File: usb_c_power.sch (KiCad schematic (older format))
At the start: 27 parts, among them J1 USB4085-GF-A, J2 ‎282837-2‎, Q1 IRF9358TRPBF, U1 CYPD3177

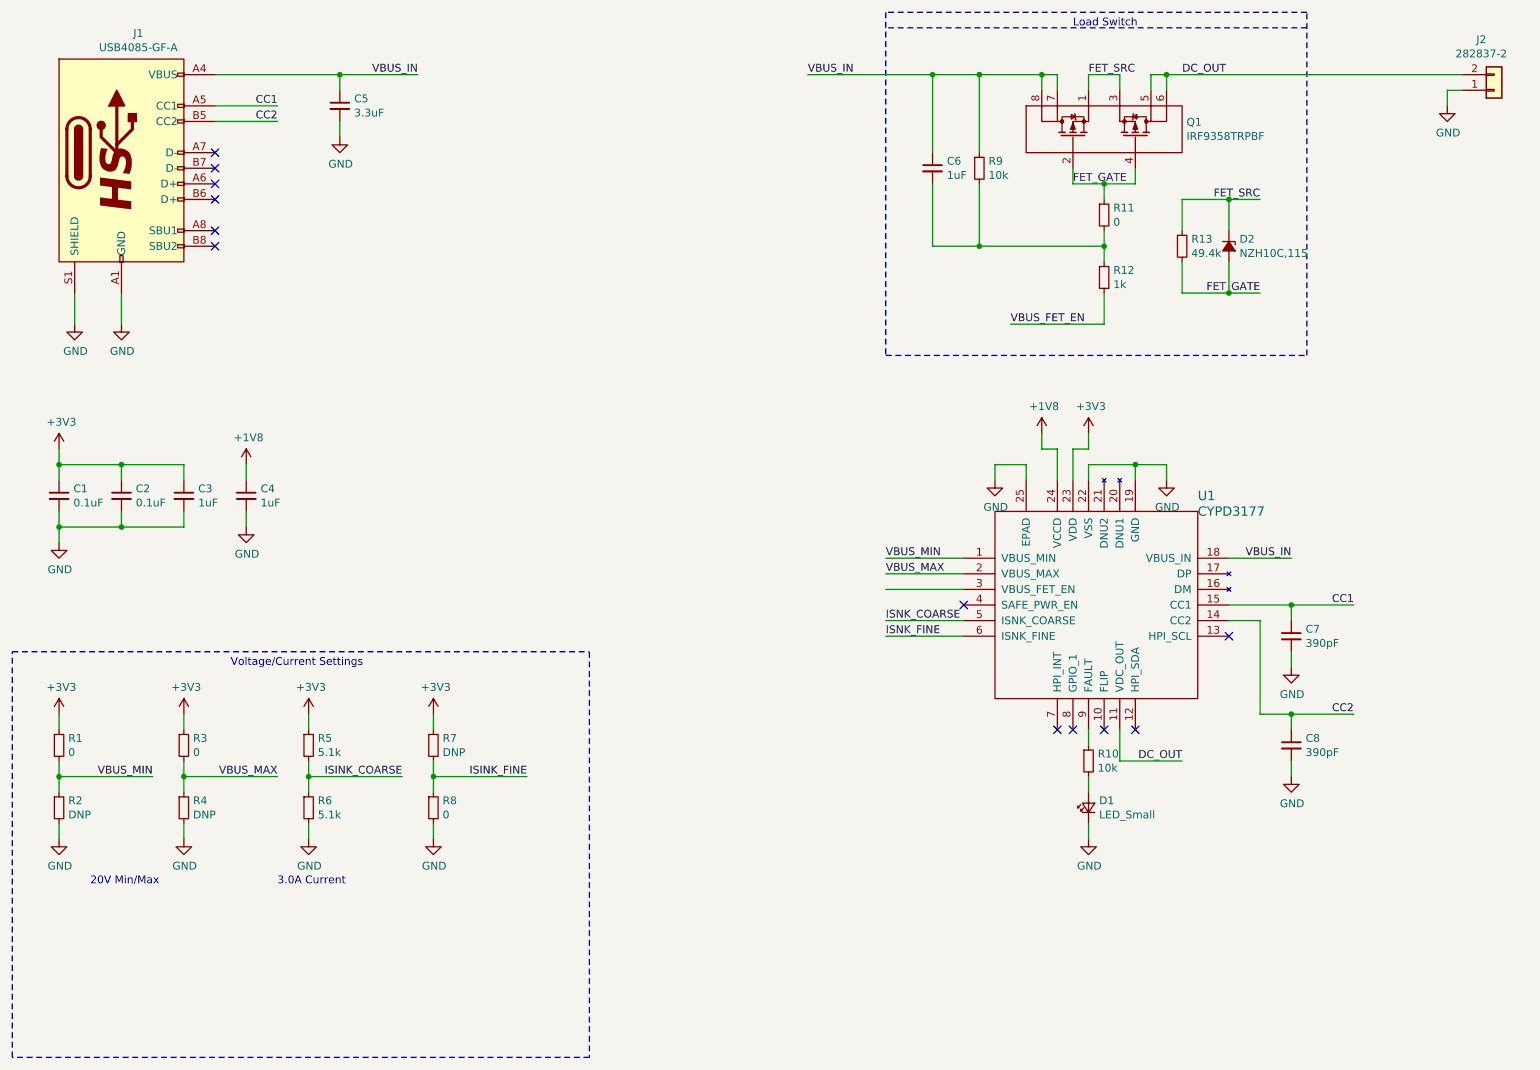
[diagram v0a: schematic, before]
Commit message: Schematic tentatively finished.
Footprints assigned and component details added
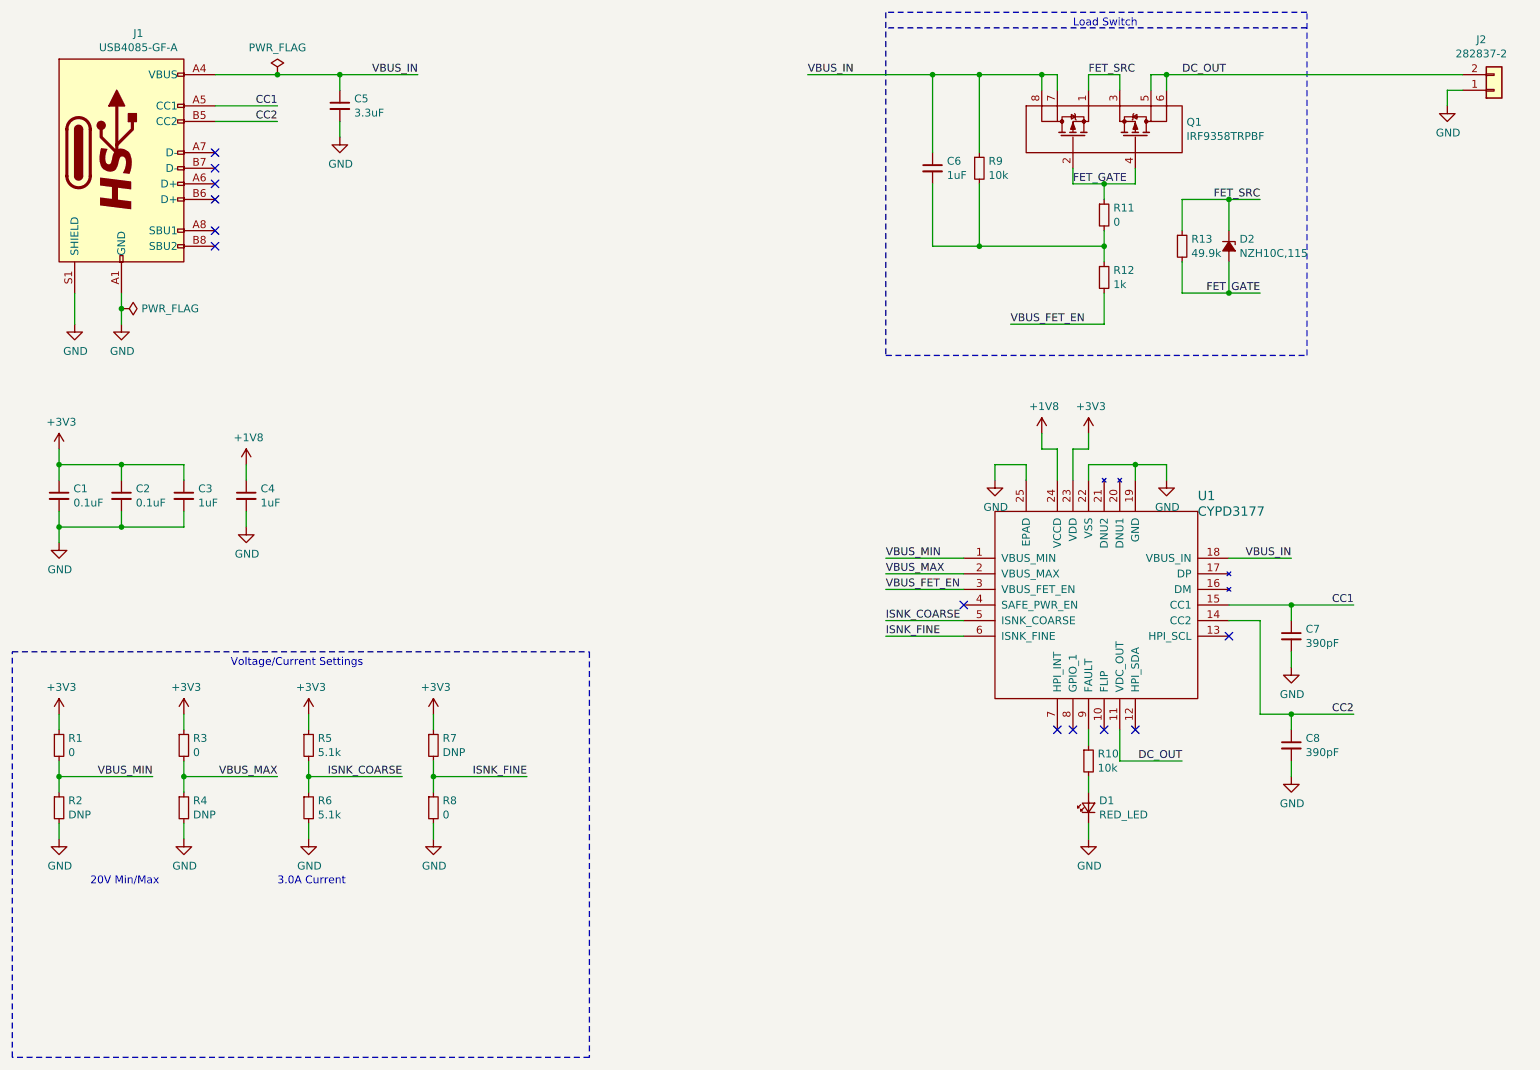
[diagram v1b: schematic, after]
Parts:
- C1, C2: footprint (none) -> Capacitor_SMD:C_0402_1005Metric; DKPN (none) -> 490-1318-1-ND; MPN (none) -> GRM155R61A104KA01D; Voltage - Rated (none) -> 10V
- C3, C4: footprint (none) -> Capacitor_SMD:C_0402_1005Metric; DKPN (none) -> 1276-1067-1-ND; MPN (none) -> CL05A105KO5NNNC; Voltage - Rated (none) -> 16V
- C5: footprint (none) -> Capacitor_SMD:C_1210_3225Metric; DKPN (none) -> 445-5716-1-ND; MPN (none) -> CGA6P3X7R1H335K250AB; Voltage - Rated (none) -> 50V
- C6: footprint (none) -> Capacitor_SMD:C_0402_1005Metric; DKPN (none) -> 445-175218-1-ND; MPN (none) -> C1005X5R1V105K050BE; Voltage - Rated (none) -> 35V
- C7, C8: footprint (none) -> Capacitor_SMD:C_0402_1005Metric; DKPN (none) -> 1276-1560-1-ND; MPN (none) -> CL05B391KB5NNNC
- D1: value LED_Small -> RED_LED; footprint (none) -> LED_SMD:LED_0603_1608Metric; DKPN (none) -> SML-D12U1WT86CT-ND; MPN (none) -> SML-D12U1WT86
- D2: footprint (none) -> Diode_SMD:D_SOD-123F; DKPN (none) -> 1727-5057-1-ND; MPN (none) -> NZH10C,115
- J1: footprint (none) -> alvarop:USB4085-GF-A; DKPN (none) -> 2073-USB4085-GF-ACT-ND; MPN (none) -> USB4085-GF-A
- J2: footprint (none) -> alvarop:‎282837-2‎; DKPN (none) -> A113320-ND; MPN (none) -> 282837-2
- Q1: footprint (none) -> Package_SO:SO-8_3.9x4.9mm_P1.27mm; DKPN (none) -> IRF9358TRPBFCT-ND; MPN (none) -> IRF9358TRPBF
- R1, R11, R3, R8: footprint (none) -> Resistor_SMD:R_0402_1005Metric; DKPN (none) -> 1276-3480-1-ND; MPN (none) -> RC1005J000CS
- R10, R9: footprint (none) -> Resistor_SMD:R_0402_1005Metric; DKPN (none) -> 311-10KJRCT-ND; MPN (none) -> RC0402JR-0710KL
- R12: footprint (none) -> Resistor_SMD:R_0402_1005Metric; DKPN (none) -> A106129CT-ND; MPN (none) -> CRG0402J1K0
- R13: value 49.4k -> 49.9k; footprint (none) -> Resistor_SMD:R_0402_1005Metric; DKPN (none) -> 311-49.9KLRCT-ND; MPN (none) -> RC0402FR-0749K9L
- R2, R4, R7: footprint (none) -> Resistor_SMD:R_0402_1005Metric
- R5, R6: footprint (none) -> Resistor_SMD:R_0402_1005Metric; DKPN (none) -> 311-5.1KJRCT-ND; MPN (none) -> RC0402JR-075K1L
- U1: footprint (none) -> Package_DFN_QFN:QFN-24-1EP_4x4mm_P0.5mm_EP2.8x2.8mm; DKPN (none) -> 428-4652-ND; MPN (none) -> CYPD3177-24LQXQ
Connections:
- net ISINK_COARSE is gone; now on net ISNK_COARSE: R5.2, R6.1
- net ISINK_FINE is gone; now on net ISNK_FINE: R7.2, R8.1
- net VBUS_FET_EN: now also U1.3 (VBUS_FET_EN)

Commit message: Created v1.1 * much larger (0805) setting resistors * 5A rated USB-C connector * Smaller 10V zener * Paste-in-hole for usb-c
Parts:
- removed J1: USB4085-GF-A, alvarop:USB4085-GF-A, symbol alvarop:USB_C_Receptacle_NODIFFPAIRS
- removed R11: 0, Resistor_SMD:R_0402_1005Metric, symbol Device:R_Small
- added J1: USB_C_Receptacle, alvarop:MOLEX-1054500101, symbol Connector:USB_C_Receptacle
- D2: footprint Diode_SMD:D_SOD-123F -> Diode_SMD:D_0402_1005Metric
- R1, R2, R3, R4, R5, R6, R7, R8: footprint Resistor_SMD:R_0402_1005Metric -> Resistor_SMD:R_0805_2012Metric_Pad1.15x1.40mm_HandSolder
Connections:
- net CC1: now also J1.A5 (CC1)
- net CC2: now also J1.B5 (CC2)
- net FET_GATE: now also C6.2, R12.1, R9.2
- net GND: now also J1.A1 (GND), J1.A12 (GND), J1.B1 (GND), J1.B12 (GND), J1.S1 (SHIELD)
- net VBUS_IN: now also J1.A4 (VBUS), J1.A9 (VBUS), J1.B4 (VBUS), J1.B9 (VBUS)
- no-connect marks 12 -> 20
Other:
- moved on the sheet: C1, C2, C3, C4

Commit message: Finished v1.1 and ordered from oshpark
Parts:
- D2: value NZH10C,115 -> BZT52C10LP-7; DKPN 1727-5057-1-ND -> BZT52C10LPDICT-ND; MPN NZH10C,115 -> BZT52C10LP-7
- R1, R3, R8: DKPN 1276-3480-1-ND -> RMCF0805ZT0R00CT-ND; MPN RC1005J000CS -> RMCF0805ZT0R00
- R5, R6: DKPN 311-5.1KJRCT-ND -> RMCF0805JT5K10CT-ND; MPN RC0402JR-075K1L -> RMCF0805JT5K10
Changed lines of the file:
@@
 Sheet 1 1
 Title "USB-C Power"
-Date "2020-03-21"
+Date "2020-03-23"
 Rev "1.1"
 Comp "alvarop.com"
@@
 P 8700 2200
 F 0 "D2" V 8654 2268 50  0000 L CNN
-F 1 "NZH10C,115" V 8745 2268 50  0000 L CNN
+F 1 "BZT52C10LP-7" V 8745 2268 50  0000 L CNN
 F 2 "Diode_SMD:D_0402_1005Metric" V 8700 2200 50  0001 C CNN
 F 3 "~" V 8700 2200 50  0001 C CNN
-F 4 "1727-5057-1-ND" H 8700 2200 50  0001 C CNN "DKPN"
-F 5 "NZH10C,115" H 8700 2200 50  0001 C CNN "MPN"
+F 4 "BZT52C10LPDICT-ND" H 8700 2200 50  0001 C CNN "DKPN"
+F 5 "BZT52C10LP-7" H 8700 2200 50  0001 C CNN "MPN"
 	1    8700 2200
 	0    1    1    0
@@
 F 2 "Resistor_SMD:R_0805_2012Metric_Pad1.15x1.40mm_HandSolder" H 1200 5400 50  0001 C CNN
 F 3 "~" H 1200 5400 50  0001 C CNN
-F 4 "1276-3480-1-ND" H 1200 5400 50  0001 C CNN "DKPN"
-F 5 "RC1005J000CS" H 1200 5400 50  0001 C CNN "MPN"
+F 4 "RMCF0805ZT0R00CT-ND" H 1200 5400 50  0001 C CNN "DKPN"
+F 5 "RMCF0805ZT0R00" H 1200 5400 50  0001 C CNN "MPN"
 	1    1200 5400
 	1    0    0    -1
@@
 F 2 "Resistor_SMD:R_0805_2012Metric_Pad1.15x1.40mm_HandSolder" H 2800 5400 50  0001 C CNN
 F 3 "~" H 2800 5400 50  0001 C CNN
-F 4 "311-5.1KJRCT-ND" H 2800 5400 50  0001 C CNN "DKPN"
-F 5 "RC0402JR-075K1L" H 2800 5400 50  0001 C CNN "MPN"
+F 4 "RMCF0805JT5K10CT-ND" H 2800 5400 50  0001 C CNN "DKPN"
+F 5 "RMCF0805JT5K10" H 2800 5400 50  0001 C CNN "MPN"
 	1    2800 5400
 	1    0    0    -1
@@
 F 2 "Resistor_SMD:R_0805_2012Metric_Pad1.15x1.40mm_HandSolder" H 2800 5800 50  0001 C CNN
 F 3 "~" H 2800 5800 50  0001 C CNN
-F 4 "311-5.1KJRCT-ND" H 2800 5800 50  0001 C CNN "DKPN"
-F 5 "RC0402JR-075K1L" H 2800 5800 50  0001 C CNN "MPN"
+F 4 "RMCF0805JT5K10CT-ND" H 2800 5800 50  0001 C CNN "DKPN"
+F 5 "RMCF0805JT5K10" H 2800 5800 50  0001 C CNN "MPN"
 	1    2800 5800
 	1    0    0    -1
@@
 F 2 "Resistor_SMD:R_0805_2012Metric_Pad1.15x1.40mm_HandSolder" H 2000 5400 50  0001 C CNN
 F 3 "~" H 2000 5400 50  0001 C CNN
-F 4 "1276-3480-1-ND" H 2000 5400 50  0001 C CNN "DKPN"
-F 5 "RC1005J000CS" H 2000 5400 50  0001 C CNN "MPN"
+F 4 "RMCF0805ZT0R00CT-ND" H 2000 5400 50  0001 C CNN "DKPN"
+F 5 "RMCF0805ZT0R00" H 2000 5400 50  0001 C CNN "MPN"
 	1    2000 5400
 	1    0    0    -1
@@
 F 2 "Resistor_SMD:R_0805_2012Metric_Pad1.15x1.40mm_HandSolder" H 3600 5800 50  0001 C CNN
 F 3 "~" H 3600 5800 50  0001 C CNN
-F 4 "1276-3480-1-ND" H 3600 5800 50  0001 C CNN "DKPN"
-F 5 "RC1005J000CS" H 3600 5800 50  0001 C CNN "MPN"
+F 4 "RMCF0805ZT0R00CT-ND" H 3600 5800 50  0001 C CNN "DKPN"
+F 5 "RMCF0805ZT0R00" H 3600 5800 50  0001 C CNN "MPN"
 	1    3600 5800
 	1    0    0    -1
